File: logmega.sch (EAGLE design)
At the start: 94 parts, among them IC1 LTC4412, IC2 4050D, IC3 ATMEGA2560-16AU, IC4 4050D, J1 POWER_JACKPTH, M0R1 ?K, M0R2 ?K, M1 FDG6342L, M1C1 ?uF, M1R1 ?K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

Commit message: begin 083_rev2
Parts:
- C11: value 100n -> 0.1uF
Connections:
- net VCC_SW_SHIELD1: no longer U$7.IOREF
- net VCC_SW_SHIELD2: now also U$7.IOREF
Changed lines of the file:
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@@
 <part name="C4" library="SmartPrj" deviceset="C-EU" device="0603-RND" value="100n"/>
 <part name="C1" library="SmartPrj" deviceset="C-EU" device="0603-RND" value="22pF"/>
-<part name="C11" library="SmartPrj" deviceset="C-EU" device="0603-RND" value="100n"/>
+<part name="C11" library="SmartPrj" deviceset="C-EU" device="0603-RND" value="0.1uF"/>
 <part name="D3" library="diode" deviceset="DIODE-" device="MINIMELF" value="CD1206-S01575"/>
 <part name="+3V5" library="supply1" deviceset="+3V3" device=""/>
@@
 <label x="-167.64" y="-208.28" size="1.778" layer="95"/>
 </segment>
+</net>
+<net name="VCC_SW_SHIELD2" class="3">
+<segment>
+<pinref part="M2" gate="G$1" pin="VOUT,C1_PIN2"/>
+<wire x1="-152.4" y1="-132.08" x2="-175.26" y2="-132.08" width="0.1524" layer="91"/>
+<label x="-175.26" y="-132.08" size="1.778" layer="95"/>
+</segment>
+<segment>
+<pinref part="U$7" gate="G$1" pin="VIN"/>
+<wire x1="-17.78" y1="-193.04" x2="12.7" y2="-193.04" width="0.1524" layer="91"/>
+<label x="-17.78" y="-193.04" size="1.778" layer="95"/>
+</segment>
+<segment>
+<pinref part="U$7" gate="G$1" pin="VCC"/>
+<wire x1="-17.78" y1="-200.66" x2="12.7" y2="-200.66" width="0.1524" layer="91"/>
+<label x="-17.78" y="-200.66" size="1.778" layer="95"/>
+</segment>
 <segment>
 <pinref part="U$7" gate="G$1" pin="IOREF"/>
@@
 </segment>
 </net>
-<net name="VCC_SW_SHIELD2" class="3">
-<segment>
-<pinref part="M2" gate="G$1" pin="VOUT,C1_PIN2"/>
-<wire x1="-152.4" y1="-132.08" x2="-175.26" y2="-132.08" width="0.1524" layer="91"/>
-<label x="-175.26" y="-132.08" size="1.778" layer="95"/>
-</segment>
-<segment>
-<pinref part="U$7" gate="G$1" pin="VIN"/>
-<wire x1="-17.78" y1="-193.04" x2="12.7" y2="-193.04" width="0.1524" layer="91"/>
-<label x="-17.78" y="-193.04" size="1.778" layer="95"/>
-</segment>
-<segment>
-<pinref part="U$7" gate="G$1" pin="VCC"/>
-<wire x1="-17.78" y1="-200.66" x2="12.7" y2="-200.66" width="0.1524" layer="91"/>
-<label x="-17.78" y="-200.66" size="1.778" layer="95"/>
-</segment>
-</net>

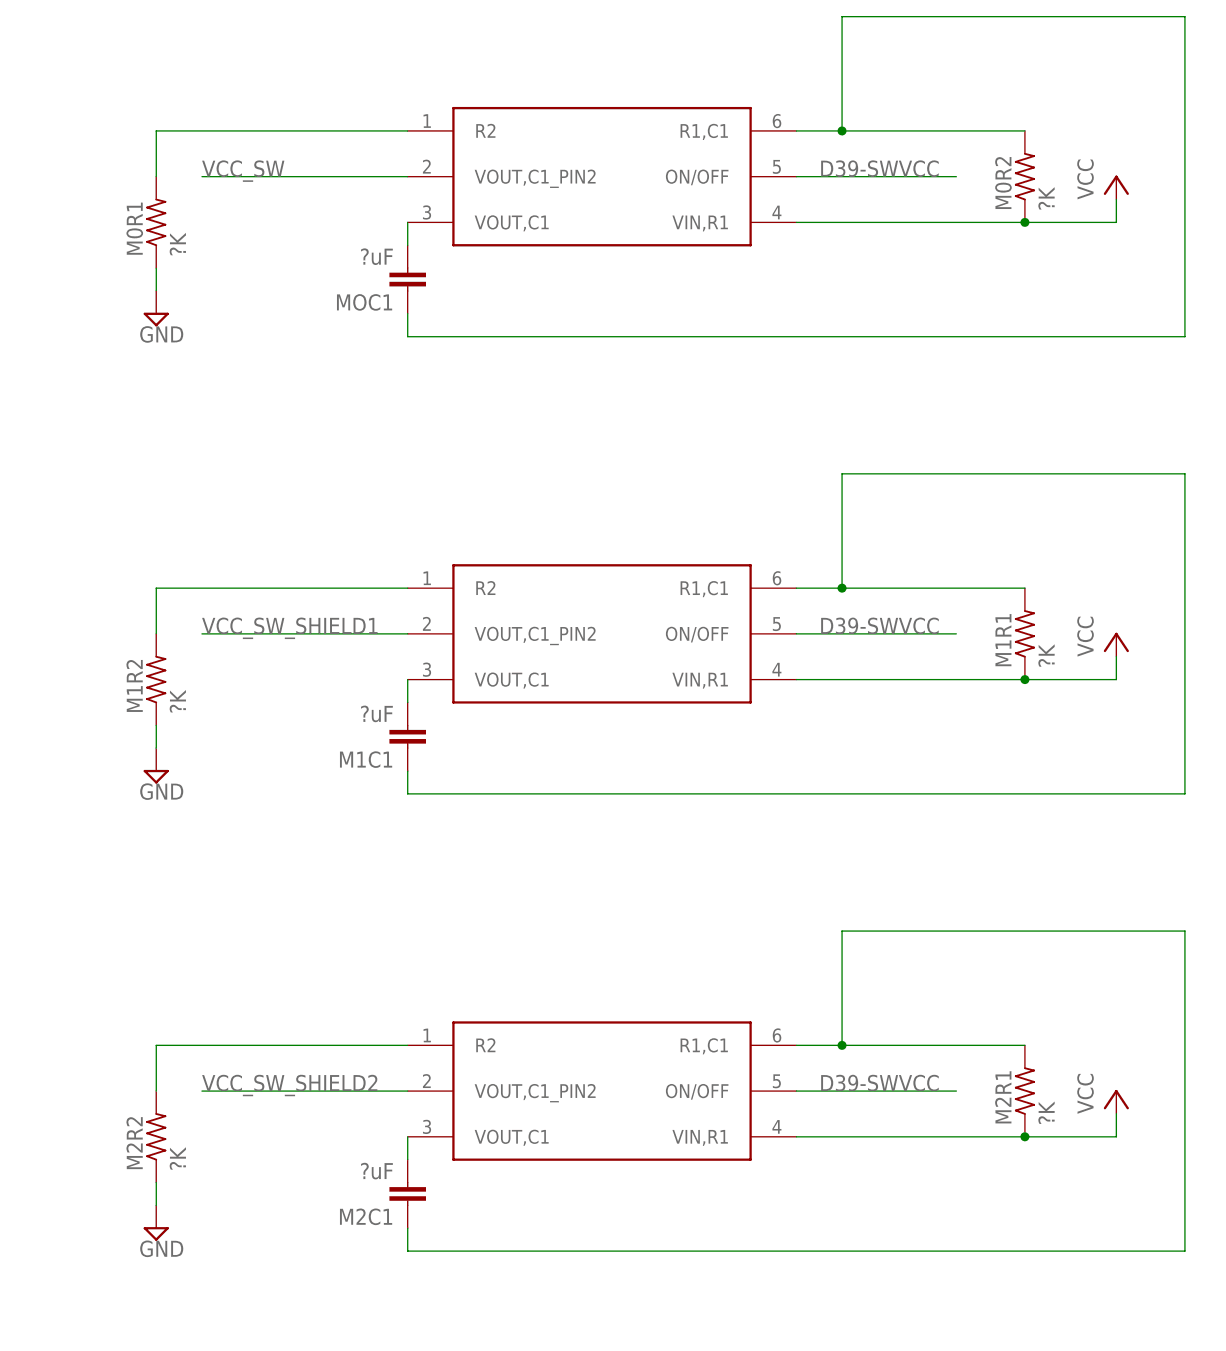
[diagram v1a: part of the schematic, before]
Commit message: Load switch resistors and capacitors labeled (#11) and CR2032 replaced with part with keepout (#3)
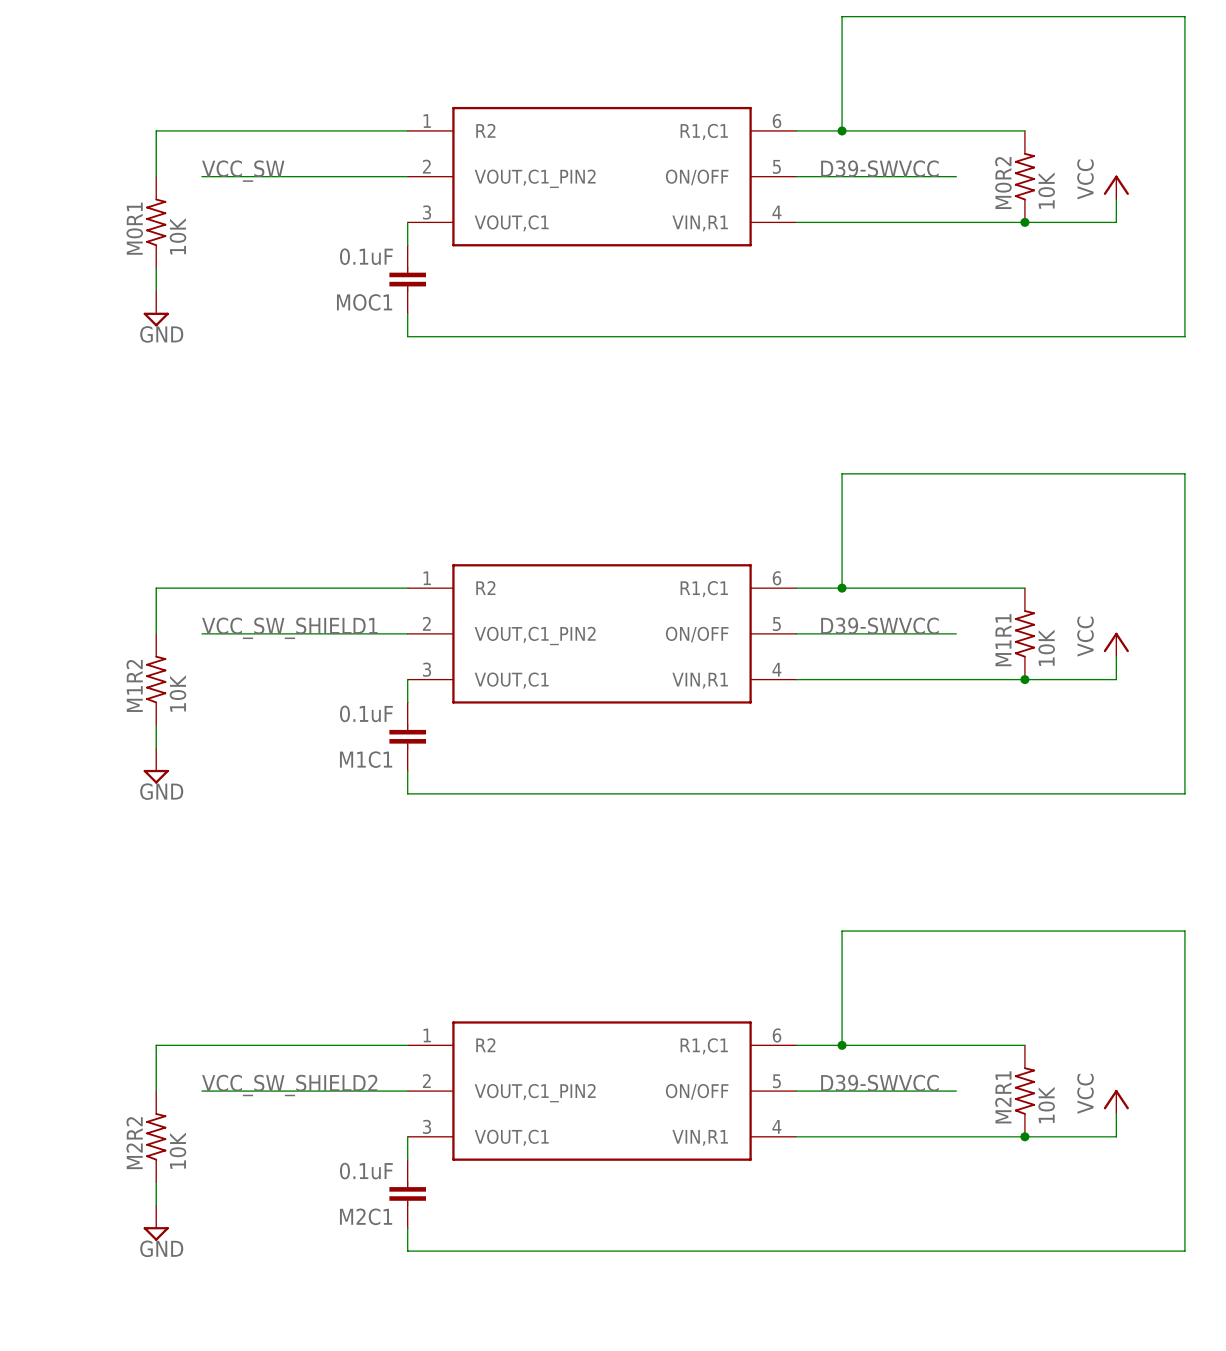
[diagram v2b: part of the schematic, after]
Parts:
- CLOCK_BATT: device adafruit:CR2032SMT -> awickert:CR2032
- M0R1, M0R2, M1R1, M1R2, M2R1, M2R2: value ?K -> 10K
- M1C1, M2C1, MOC1: value ?uF -> 0.1uF
- renumbered SW to M0/SW
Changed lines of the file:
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@@
 <part name="SUPPLY9" library="supply2" deviceset="GND" device=""/>
 <part name="SD" library="adafruit" deviceset="SDMMC" device="06132"/>
-<part name="CLOCK_BATT" library="adafruit" deviceset="CR2032" device="SMT" value="3V Backup Battery"/>
+<part name="CLOCK_BATT" library="awickert" deviceset="CR2032" device="" value="3V Backup Battery"/>
 <part name="JP2" library="SparkFun" deviceset="STAND-OFF" device=""/>
 <part name="JP3" library="SparkFun" deviceset="STAND-OFF" device=""/>
@@
 <part name="VCC_VDIV_2" library="rcl" deviceset="R-US_" device="R0603" value="1M"/>
 <part name="SUPPLY44" library="supply2" deviceset="GND" device=""/>
-<part name="SW" library="awickert" deviceset="FDG6342L" device=""/>
+<part name="M0/SW" library="awickert" deviceset="FDG6342L" device=""/>
 <part name="P+10" library="supply1" deviceset="VCC" device=""/>
-<part name="M0R1" library="rcl" deviceset="R-US_" device="R0603" value="?K"/>
+<part name="M0R1" library="rcl" deviceset="R-US_" device="R0603" value="10K"/>
 <part name="SUPPLY45" library="supply2" deviceset="GND" device=""/>
-<part name="M0R2" library="rcl" deviceset="R-US_" device="R0603" value="?K"/>
-<part name="MOC1" library="resistor" deviceset="C-EU" device="C0603" value="?uF"/>
+<part name="M0R2" library="rcl" deviceset="R-US_" device="R0603" value="10K"/>
+<part name="MOC1" library="resistor" deviceset="C-EU" device="C0603" value="0.1uF"/>
 <part name="R_REF_A8" library="resistor" deviceset="R-US_" device="0207/10" value="Therm"/>
 <part name="R_REF_A9" library="resistor" deviceset="R-US_" device="0207/10"/>
@@
 <part name="M1" library="awickert" deviceset="FDG6342L" device=""/>
 <part name="P+16" library="supply1" deviceset="VCC" device=""/>
-<part name="M1R2" library="rcl" deviceset="R-US_" device="R0603" value="?K"/>
+<part name="M1R2" library="rcl" deviceset="R-US_" device="R0603" value="10K"/>
 <part name="SUPPLY60" library="supply2" deviceset="GND" device=""/>
-<part name="M1R1" library="rcl" deviceset="R-US_" device="R0603" value="?K"/>
-<part name="M1C1" library="resistor" deviceset="C-EU" device="C0603" value="?uF"/>
+<part name="M1R1" library="rcl" deviceset="R-US_" device="R0603" value="10K"/>
+<part name="M1C1" library="resistor" deviceset="C-EU" device="C0603" value="0.1uF"/>
 <part name="M2" library="awickert" deviceset="FDG6342L" device=""/>
 <part name="P+22" library="supply1" deviceset="VCC" device=""/>
-<part name="M2R2" library="rcl" deviceset="R-US_" device="R0603" value="?K"/>
+<part name="M2R2" library="rcl" deviceset="R-US_" device="R0603" value="10K"/>
 <part name="SUPPLY61" library="supply2" deviceset="GND" device=""/>
-<part name="M2R1" library="rcl" deviceset="R-US_" device="R0603" value="?K"/>
-<part name="M2C1" library="resistor" deviceset="C-EU" device="C0603" value="?uF"/>
+<part name="M2R1" library="rcl" deviceset="R-US_" device="R0603" value="10K"/>
+<part name="M2C1" library="resistor" deviceset="C-EU" device="C0603" value="0.1uF"/>
 <part name="H1" library="SparkFun" deviceset="M08" device="3.5MM-8"/>
 <part name="+3V1" library="supply1" deviceset="+3V3" device=""/>
@@
 <instance part="VCC_VDIV_2" gate="G$1" x="45.72" y="-182.88" rot="MR90"/>
 <instance part="SUPPLY44" gate="GND" x="45.72" y="-193.04" rot="MR0"/>
-<instance part="SW" gate="G$1" x="-129.54" y="-30.48"/>
+<instance part="M0/SW" gate="G$1" x="-129.54" y="-30.48"/>
 <instance part="P+10" gate="VCC" x="-73.66" y="-30.48"/>
 <instance part="M0R1" gate="G$1" x="-180.34" y="-35.56" rot="R90"/>
@@
 </segment>
 <segment>
-<pinref part="SW" gate="G$1" pin="VIN,R1"/>
+<pinref part="M0/SW" gate="G$1" pin="VIN,R1"/>
 <wire x1="-109.22" y1="-35.56" x2="-83.82" y2="-35.56" width="0.1524" layer="91"/>
 <wire x1="-83.82" y1="-35.56" x2="-73.66" y2="-35.56" width="0.1524" layer="91"/>
@@
 </segment>
 <segment>
-<pinref part="SW" gate="G$1" pin="ON/OFF"/>
+<pinref part="M0/SW" gate="G$1" pin="ON/OFF"/>
 <wire x1="-109.22" y1="-30.48" x2="-91.44" y2="-30.48" width="0.1524" layer="91"/>
 <label x="-106.68" y="-30.48" size="1.778" layer="95"/>
@@
 <net name="N$13" class="0">
 <segment>
-<pinref part="SW" gate="G$1" pin="R2"/>
+<pinref part="M0/SW" gate="G$1" pin="R2"/>
 <wire x1="-152.4" y1="-25.4" x2="-180.34" y2="-25.4" width="0.1524" layer="91"/>
 <wire x1="-180.34" y1="-25.4" x2="-180.34" y2="-30.48" width="0.1524" layer="91"/>
@@
 <net name="N$14" class="0">
 <segment>
-<pinref part="SW" gate="G$1" pin="R1,C1"/>
+<pinref part="M0/SW" gate="G$1" pin="R1,C1"/>
 <pinref part="M0R2" gate="G$1" pin="2"/>
 <wire x1="-109.22" y1="-25.4" x2="-104.14" y2="-25.4" width="0.1524" layer="91"/>
@@
 <net name="N$10" class="0">
 <segment>
-<pinref part="SW" gate="G$1" pin="VOUT,C1"/>
+<pinref part="M0/SW" gate="G$1" pin="VOUT,C1"/>
 <pinref part="MOC1" gate="G$1" pin="2"/>
 <wire x1="-152.4" y1="-38.1" x2="-152.4" y2="-35.56" width="0.1524" layer="91"/>
@@
 <net name="VCC_SW" class="0">
 <segment>
-<pinref part="SW" gate="G$1" pin="VOUT,C1_PIN2"/>
+<pinref part="M0/SW" gate="G$1" pin="VOUT,C1_PIN2"/>
 <wire x1="-152.4" y1="-30.48" x2="-175.26" y2="-30.48" width="0.1524" layer="91"/>
 <label x="-175.26" y="-30.48" size="1.778" layer="95"/>

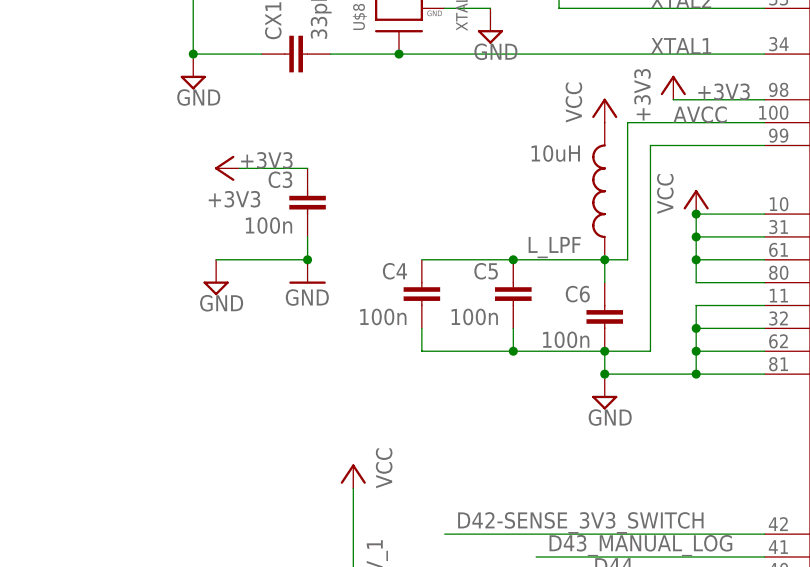
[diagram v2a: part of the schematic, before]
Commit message: Multiple silkscreen and value label changes: #13 #16 #18 #20
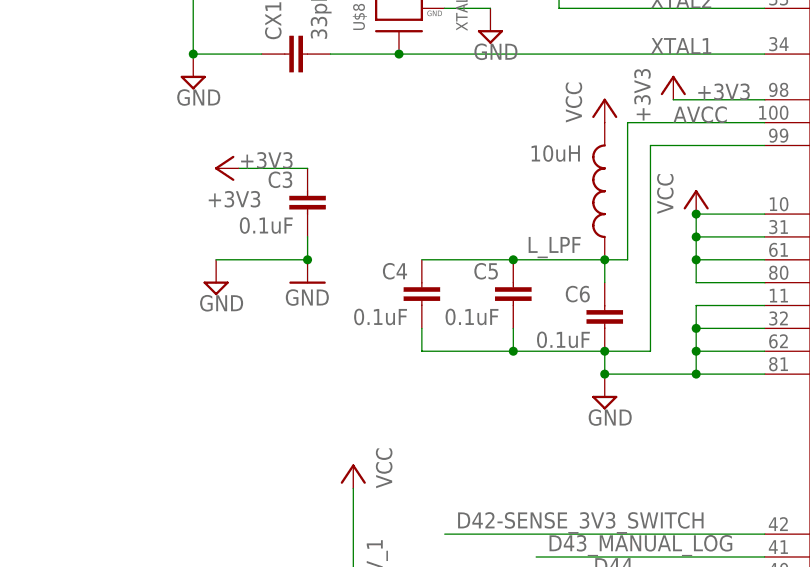
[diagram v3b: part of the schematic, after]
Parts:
- C3, C4, C5, C6: value 100n -> 0.1uF
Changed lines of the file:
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@@
 <part name="SUPPLY16" library="supply2" deviceset="GND" device=""/>
 <part name="+3V3" library="supply1" deviceset="+3V3" device=""/>
-<part name="C3" library="SmartPrj" deviceset="C-EU" device="0603-RND" value="100n"/>
+<part name="C3" library="SmartPrj" deviceset="C-EU" device="0603-RND" value="0.1uF"/>
 <part name="GND8" library="supply1" deviceset="GND" device=""/>
-<part name="C6" library="SmartPrj" deviceset="C-EU" device="0603-RND" value="100n"/>
+<part name="C6" library="SmartPrj" deviceset="C-EU" device="0603-RND" value="0.1uF"/>
 <part name="IC3" library="SmartPrj" deviceset="ATMEGA2560" device="AU" technology="2560-16" value="ATMEGA2560-16AU"/>
-<part name="C5" library="SmartPrj" deviceset="C-EU" device="0603-RND" value="100n"/>
-<part name="C4" library="SmartPrj" deviceset="C-EU" device="0603-RND" value="100n"/>
+<part name="C5" library="SmartPrj" deviceset="C-EU" device="0603-RND" value="0.1uF"/>
+<part name="C4" library="SmartPrj" deviceset="C-EU" device="0603-RND" value="0.1uF"/>
 <part name="C1" library="SmartPrj" deviceset="C-EU" device="0603-RND" value="22pF"/>
 <part name="C11" library="SmartPrj" deviceset="C-EU" device="0603-RND" value="0.1uF"/>
